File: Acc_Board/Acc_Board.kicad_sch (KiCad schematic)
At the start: 43 parts, among them J1 1053091202, J11 1053091202, J12 776087-1, J2 1053091202, J3 1053091202, J4 1053091202, J5 1053091202, J6 1053091202, J9 1053091202, K1 Relay_SPST-NO, U1 ISO1050DUB, U13 R-78B5.0-2.0, U2 NUCLEO-L432KC, U4 PQDE6W-Q110-S5-H-D

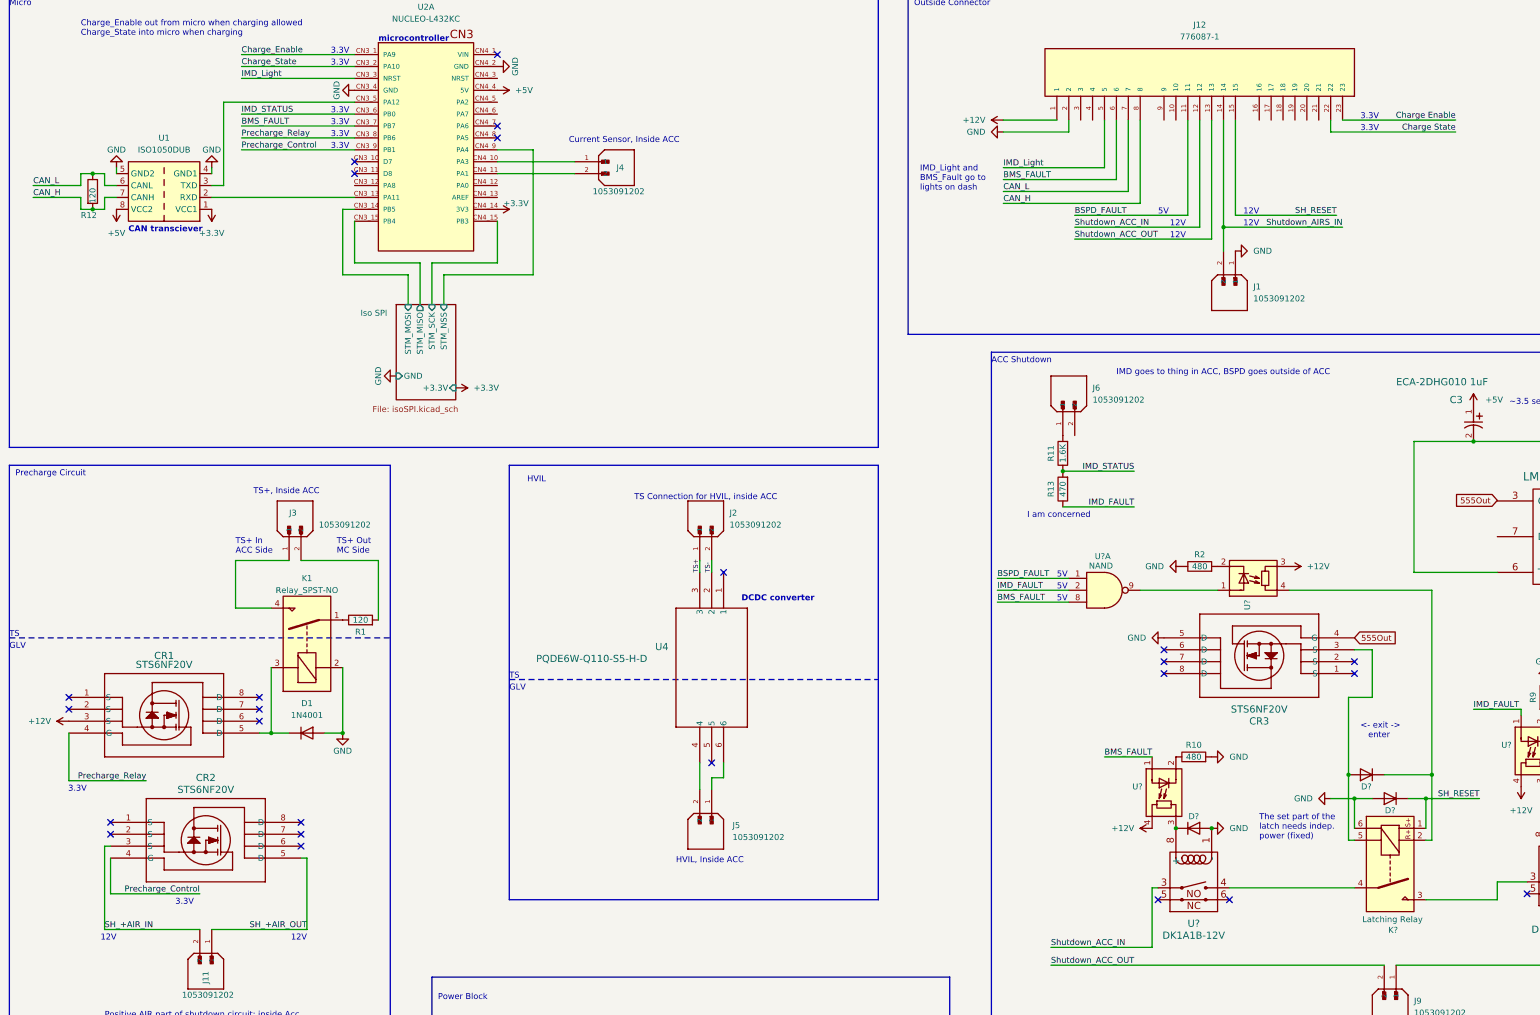
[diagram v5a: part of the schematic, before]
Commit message: added notes to parts of the board that need changing
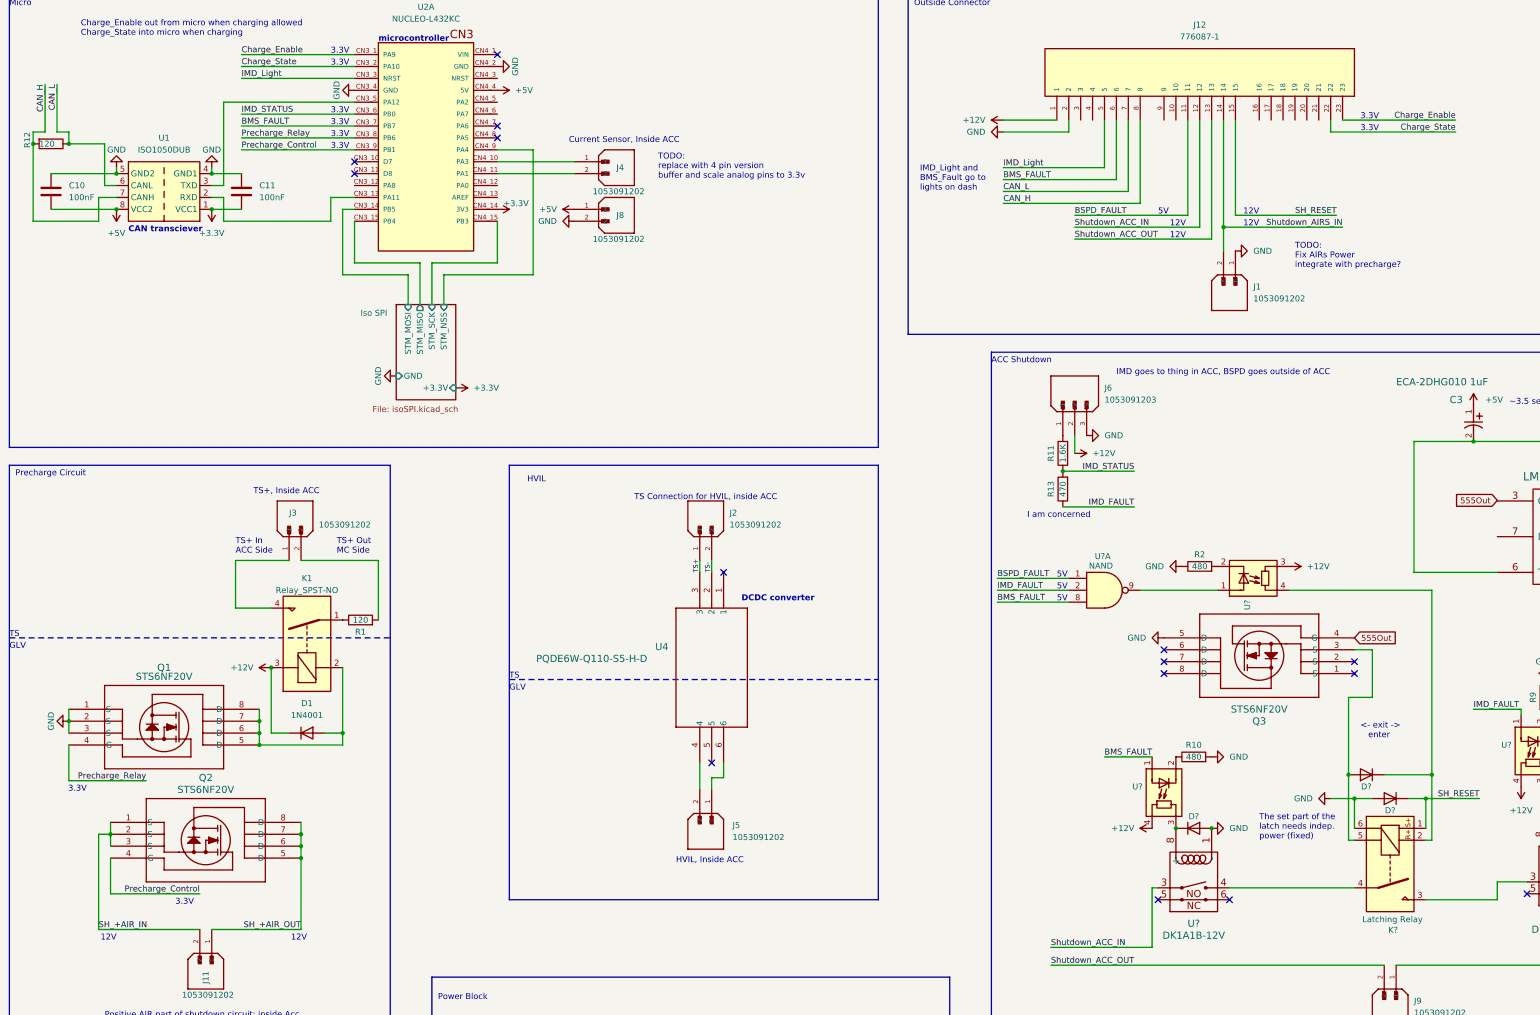
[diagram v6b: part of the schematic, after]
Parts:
- removed J6: 1053091202, 1FS_2_Global_Footprint_Library:MOLEX_1053091202, symbol molex_1053091202:1053091202
- added C10, C11: 100nF, symbol Device:C
- added J6: 1053091203, 1053091203:MOLEX_1053091203, symbol 1FS_2_Global_Symbol_Library:1053091203
- added J8: 1053091202, 1FS_2_Global_Footprint_Library:MOLEX_1053091202, symbol molex_1053091202:1053091202
- renumbered CR1 to Q1, CR2 to Q2, CR3 to Q3
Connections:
- net Charge Enable is gone; now on net Charge_Enable: J12.23
- net Charge State is gone; now on net Charge_State: J12.22
- net +12V: now also D1.1 (K), K1.3, J6.2; no longer Q1.3 (S)
- net +3.3V: now also C11.2
- net +5V: now also C10.2, J8.1
- net GND: now also Q1.1 (S), Q1.2 (S), Q1.3 (S), C10.1, C11.1, J6.3, J8.2; no longer D1.2 (A), K1.2
- net SH_+AIR_IN: now also Q2.1 (S), Q2.2 (S)
- net SH_+AIR_OUT: now also Q2.6 (D), Q2.7 (D), Q2.8 (D)
- net at R11.2: now also J6.1
- net at Q1.6 (D): now also D1.2 (A), K1.2, Q1.5 (D), Q1.7 (D), Q1.8 (D)
- no-connect marks 26 -> 16
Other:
- note added: "TODO: Fix AIRs Power integrate with precharge?"
- note added: "TODO: replace with 4 pin version buffer and scale analog pins to 3.3v"
- moved on the sheet: Q1, R12

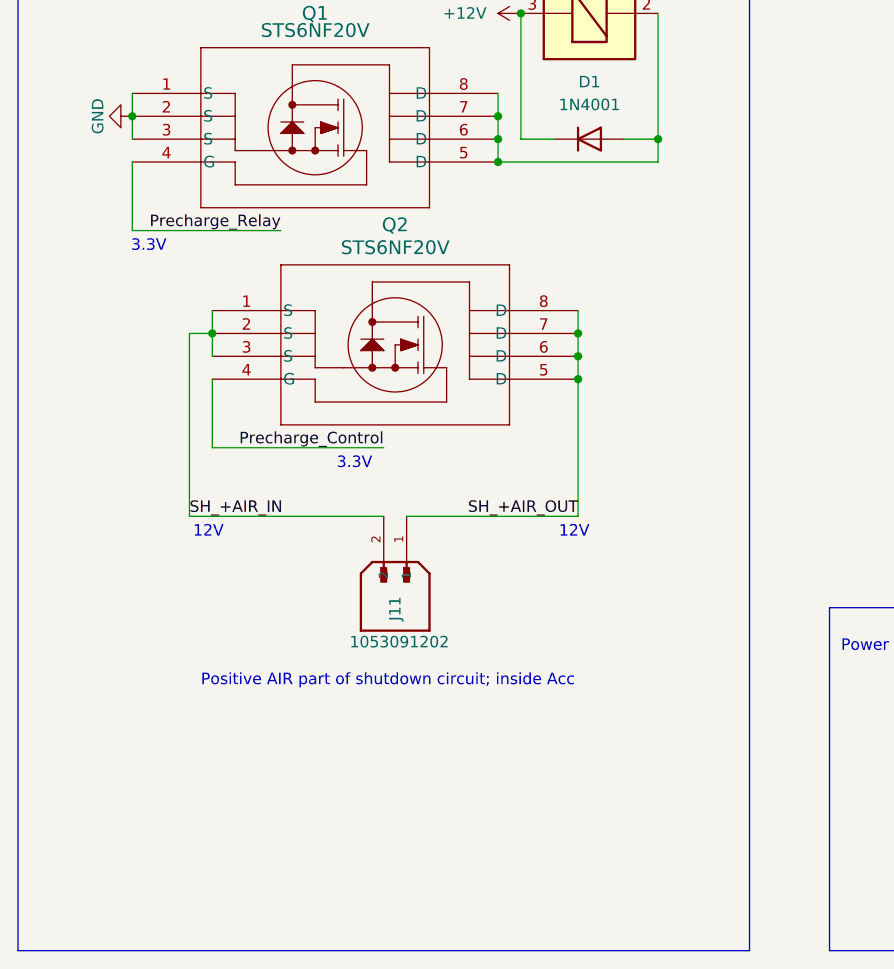
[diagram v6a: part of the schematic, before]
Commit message: fixed mosfets on acc board
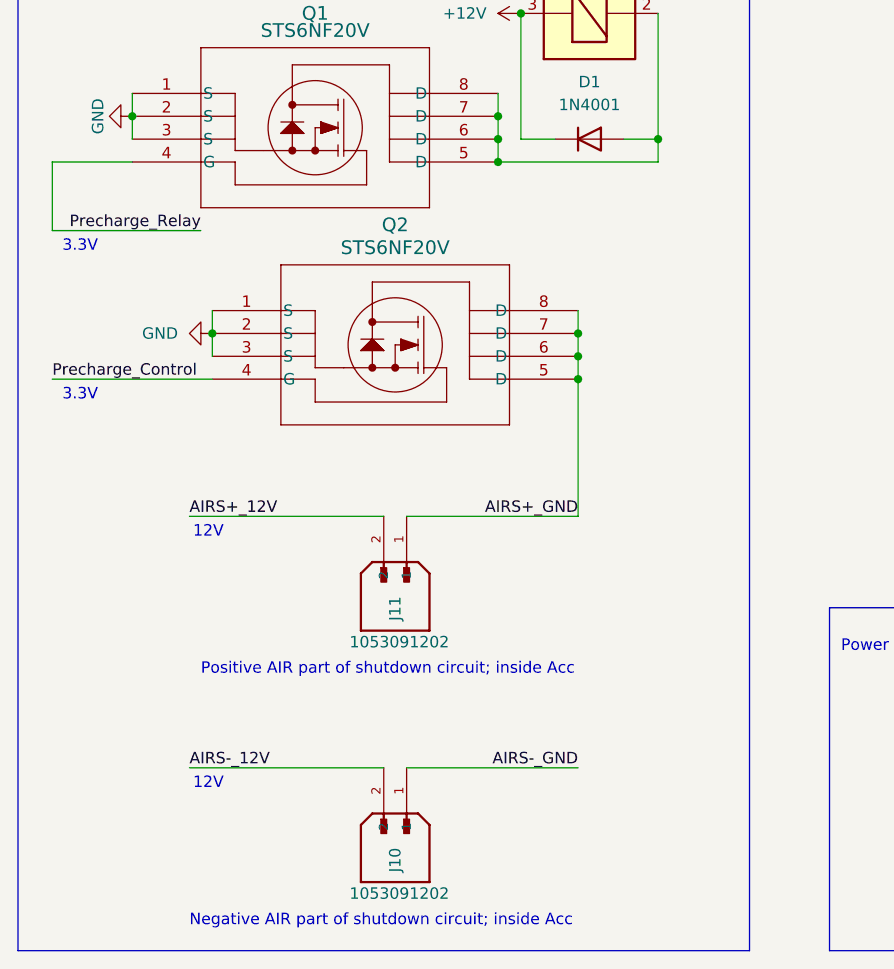
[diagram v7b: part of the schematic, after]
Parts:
- added J10: 1053091202, 1FS_2_Global_Footprint_Library:MOLEX_1053091202, symbol molex_1053091202:1053091202
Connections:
- net GND: now also Q2.1 (S), Q2.2 (S), Q2.3 (S)
- removed net SH_+AIR_IN: J11.2, Q2.1 (S), Q2.2 (S), Q2.3 (S)
- net SH_+AIR_OUT renamed AIRS+_GND
- new net AIRS+_12V: J11.2
- new net AIRS-_12V: J10.2
- new net AIRS-_GND: J10.1
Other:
- note added: "Negative AIR part of shutdown circuit; inside Acc"
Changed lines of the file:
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@@
     (stroke (width 1) (type default))
   )
-  (wire (pts (xy 35.56 182.88) (xy 35.56 175.26))
+  (wire (pts (xy 26.67 182.88) (xy 26.67 175.26))
     (stroke (width 0) (type default))
   )
@@
     (stroke (width 0) (type default))
   )
-  (wire (pts (xy 41.91 194.31) (xy 44.45 194.31))
-    (stroke (width 0) (type default))
-  )
   (wire (pts (xy 340.36 204.47) (xy 346.71 204.47))
     (stroke (width 1) (type default))
   )
-  (wire (pts (xy 63.5 207.01) (xy 44.45 207.01))
-    (stroke (width 0) (type default))
-  )
   (wire (pts (xy 326.39 142.24) (xy 295.91 142.24))
     (stroke (width 0) (type default))
@@
     (stroke (width 0) (type default))
   )
-  (wire (pts (xy 41.91 214.63) (xy 41.91 194.31))
-    (stroke (width 0) (type default))
-  )
   (wire (pts (xy 76.2 170.18) (xy 76.2 172.72))
     (stroke (width 0) (type default))
@@
     (stroke (width 0) (type default))
   )
+  (wire (pts (xy 63.5 242.57) (xy 41.91 242.57))
+    (stroke (width 0) (type default))
+  )
   (wire (pts (xy 245.11 218.44) (xy 266.7 218.44))
     (stroke (width 1) (type default))
@@
     (stroke (width 0) (type default))
   )
+  (wire (pts (xy 66.04 242.57) (xy 85.09 242.57))
+    (stroke (width 0) (type default))
+  )
   (wire (pts (xy 256.54 177.8) (xy 266.7 177.8))
     (stroke (width 0) (type default))
@@
     (stroke (width 0) (type default))
   )
+  (wire (pts (xy 26.67 199.39) (xy 44.45 199.39))
+    (stroke (width 0) (type default))
+  )
   (wire (pts (xy 234.95 57.15) (xy 261.62 57.15))
     (stroke (width 0) (type default))
@@
     (stroke (width 0) (type default))
   )
-  (wire (pts (xy 44.45 199.39) (xy 44.45 207.01))
-    (stroke (width 0) (type default))
-  )
   (wire (pts (xy 72.39 43.18) (xy 96.52 43.18))
     (stroke (width 0) (type default))
@@
     (stroke (width 0) (type default))
   )
+  (wire (pts (xy 26.67 175.26) (xy 35.56 175.26))
+    (stroke (width 0) (type default))
+  )
   (wire (pts (xy 93.98 60.96) (xy 96.52 60.96))
     (stroke (width 0) (type default))
@@
     (stroke (width 0) (type default))
   )
-  (wire (pts (xy 52.07 182.88) (xy 35.56 182.88))
+  (wire (pts (xy 43.18 182.88) (xy 26.67 182.88))
     (stroke (width 0) (type default))
   )
@@
     (effects (font (size 1.27 1.27)) (justify right bottom))
   )
-  (text "3.3V" (at 39.37 185.42 0)
+  (text "3.3V" (at 31.75 185.42 0)
     (effects (font (size 1.27 1.27)) (justify right bottom))
   )
@@
     (effects (font (size 1.27 1.27)) (justify left bottom))
   )
+  (text "Negative AIR part of shutdown circuit; inside Acc" (at 41.91 260.35 0)
+    (effects (font (size 1.27 1.27)) (justify left bottom))
+  )
   (text "TODO:\nFix AIRs Power\nintegrate with precharge?" (at 297.18 73.66 0)
     (effects (font (size 1.27 1.27)) (justify left bottom))
@@
     (effects (font (size 1.27 1.27)) (justify left bottom))
   )
-  (text "12V" (at 86.36 217.17 0)
-    (effects (font (size 1.27 1.27)) (justify right bottom))
-  )
   (text "TS Connection for HVIL, inside ACC" (at 156.21 123.19 0)
     (effects (font (size 1.27 1.27)) (justify left bottom))
@@
     (effects (font (size 1.27 1.27)) (justify right bottom))
   )
-  (text "3.3V" (at 62.23 209.55 0)
+  (text "3.3V" (at 31.75 201.93 0)
     (effects (font (size 1.27 1.27)) (justify right bottom))
   )
@@
     (effects (font (size 1.27 1.27)) (justify left bottom))
   )
-  (text "Positive AIR part of shutdown circuit; inside Acc" (at 43.18 233.68 0)
+  (text "Positive AIR part of shutdown circuit; inside Acc" (at 43.18 232.41 0)
     (effects (font (size 1.27 1.27)) (justify left bottom))
   )
@@
     (effects (font (size 1.27 1.27)) (justify left bottom))
   )
+  (text "12V" (at 45.72 245.11 0)
+    (effects (font (size 1.27 1.27)) (justify right bottom))
+  )
   (text "12V" (at 270.51 64.77 0)
     (effects (font (size 1.27 1.27)) (justify left bottom))
@@
     (effects (font (size 1.27 1.27)) (justify left bottom))
   )
+  (label "AIRS-_12V" (at 41.91 242.57 0) (fields_autoplaced)
+    (effects (font (size 1.27 1.27)) (justify left bottom))
+  )
   (label "CAN_H" (at 234.95 59.69 0) (fields_autoplaced)
     (effects (font (size 1.27 1.27)) (justify left bottom))
@@
     (effects (font (size 1.27 1.27)) (justify left bottom))
   )
-  (label "Precharge_Relay" (at 52.07 182.88 180) (fields_autoplaced)
+  (label "Precharge_Relay" (at 43.18 182.88 180) (fields_autoplaced)
+    (effects (font (size 1.27 1.27)) (justify right bottom))
+  )
+  (label "AIRS-_GND" (at 85.09 242.57 180) (fields_autoplaced)
     (effects (font (size 1.27 1.27)) (justify right bottom))
   )
@@
     (effects (font (size 1 1)) (justify left bottom))
   )
-  (label "Precharge_Control" (at 63.5 207.01 180) (fields_autoplaced)
-    (effects (font (size 1.27 1.27)) (justify right bottom))
+  (label "Precharge_Control" (at 26.67 199.39 0) (fields_autoplaced)
+    (effects (font (size 1.27 1.27)) (justify left bottom))
   )
   (label "BSPD_FAULT" (at 233.68 139.7 0) (fields_autoplaced)
@@
     (effects (font (size 1.27 1.27)) (justify right bottom))
   )
-  (label "SH_+AIR_IN" (at 41.91 214.63 0) (fields_autoplaced)
+  (label "AIRS+_12V" (at 41.91 214.63 0) (fields_autoplaced)
     (effects (font (size 1.27 1.27)) (justify left bottom))
   )
-  (label "SH_+AIR_OUT" (at 85.09 214.63 180) (fields_autoplaced)
+  (label "AIRS+_GND" (at 85.09 214.63 180) (fields_autoplaced)
     (effects (font (size 1.27 1.27)) (justify right bottom))
   )
@@
     )
   )
+  (symbol (lib_id "power:GND") (at 44.45 194.31 270) (unit 1)
+    (in_bom yes) (on_board yes) (dnp no) (fields_autoplaced)
+    (property "Reference" "#PWR049" (at 38.1 194.31 0)
+      (effects (font (size 1.27 1.27)) hide)
+    )
+    (property "Value" "GND" (at 40.64 194.31 90)
+      (effects (font (size 1.27 1.27)) (justify right))
+    )
+    (property "Footprint" "" (at 44.45 194.31 0)
+      (effects (font (size 1.27 1.27)) hide)
+    )
+    (property "Datasheet" "" (at 44.45 194.31 0)
+      (effects (font (size 1.27 1.27)) hide)
+    )
+    (pin "1")
+    (instances
+      (project "Acc_Board"
+        (path "/e19d26dd-723b-45e6-9d59-b1730158e759"
+          (reference "#PWR049") (unit 1)
+        )
+      )
+    )
+  )
   (symbol (lib_id "1_ACC_BOARD:STS6NF20V") (at 309.88 160.02 180) (unit 1)
     (in_bom yes) (on_board yes) (dnp no) (fields_autoplaced)
@@
         )
       )
+    )
+  )
+  (symbol (lib_id "molex_1053091202:1053091202") (at 66.04 247.65 270) (unit 1)
+    (in_bom yes) (on_board yes) (dnp no)
+    (property "Reference" "J10" (at 64.77 251.46 0)
+      (effects (font (size 1.27 1.27)) (justify left))
+    )
+    (property "Value" "1053091202" (at 59.69 256.54 90)
+      (effects (font (size 1.27 1.27)) (justify left))
+    )
+    (property "Footprint" "1FS_2_Global_Footprint_Library:MOLEX_1053091202" (at 66.04 247.65 0)
+      (effects (font (size 1.27 1.27)) (justify bottom) hide)
+    )
+    (property "Datasheet" "" (at 66.04 247.65 0)
+      (effects (font (size 1.27 1.27)) hide)
+    )
+    (property "PARTREV" "H" (at 66.04 247.65 0)
+      (effects (font (size 1.27 1.27)) (justify bottom) hide)
+    )
+    (property "STANDARD" "Manufacturer Recommendations" (at 66.04 247.65 0)
+      (effects (font (size 1.27 1.27)) (justify bottom) hide)
+    )
+    (property "MAXIMUM_PACKAGE_HEIGHT" "10.51 mm" (at 66.04 247.65 0)
+      (effects (font (size 1.27 1.27)) (justify bottom) hide)
+    )
+    (property "MANUFACTURER" "Molex" (at 66.04 247.65 0)
+      (effects (font (size 1.27 1.27)) (justify bottom) hide)
+    )
+    (pin "1")
+    (pin "2")
+    (instances
+      (project "Acc_Board"
+        (path "/e19d26dd-723b-45e6-9d59-b1730158e759"
+          (reference "J10") (unit 1)
+        )
+      )
+      (project "Precharge"
+        (path "/ebbe473b-926f-45d4-8349-621c37aa98bc"
+          (reference "J?") (unit 1)
+        )
+      )

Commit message: Minor acc board changes
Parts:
- removed J4, J8: 1053091202, 1FS_2_Global_Footprint_Library:MOLEX_1053091202, symbol molex_1053091202:1053091202
- added C12, C9: 10µF, symbol Device:C
- added J13: 1053091204, 1FS_2_Global_Footprint_Library:MOLEX_1053091204, symbol 1FS_2_Global_Symbol_Library:1053091204
- C1, C2, C7, C8: footprint Capacitor_SMD:C_0805_2012Metric_Pad1.18x1.45mm_HandSolder -> (none)
- C3: footprint PCAP_63x112_PAN -> (none)
- D1, D? (x4): footprint Diode_THT:D_DO-41_SOD81_P10.16mm_Horizontal -> (none)
- J6: footprint 1053091203:MOLEX_1053091203 -> 1FS_2_Global_Footprint_Library:MOLEX_1053091203
- R10, R11, R12, R13, R2, R9: footprint Resistor_SMD:R_0805_2012Metric_Pad1.20x1.40mm_HandSolder -> (none)
- R?: footprint Resistor_THT:R_Axial_DIN0207_L6.3mm_D2.5mm_P10.16mm_Horizontal -> (none)
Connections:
- net +5V: now also J13.3
- net GND: now also J13.4
- net TS+: now also C12.1
- net TS-: now also C12.2
- net at U2.CN4_10 (PA3): now also J13.1
- net at U2.CN4_11 (PA1): now also J13.2
- net at J5.1, U4.6: now also C9.2
- net at J5.2, U4.4: now also C9.1
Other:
- note added: "TODO: buffer and scale analog pins to 3.3v"
- note removed: "TODO: replace with 4 pin version buffer and scale analog pins to 3.3v"
- moved on the sheet: J2, J5, U4
